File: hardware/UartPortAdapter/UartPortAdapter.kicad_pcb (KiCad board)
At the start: 2 copper layers, 16.5 x 19.5 mm, 3 parts, among them J1 Mid Expansion Header, J2 FTDI

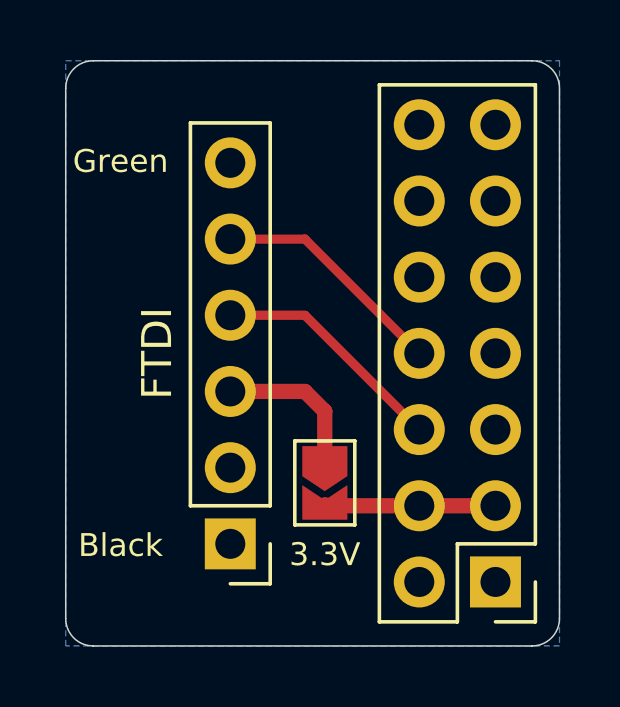
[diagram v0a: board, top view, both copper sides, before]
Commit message: Fixed the UART adapter PCB
The 0.1" 2x7 Mid Expansion header was flipped left to right. I noticed
this issue when testing revision 0.1.0 of the PCB.

This updated version has been sent off to OSHPark for manufacture.
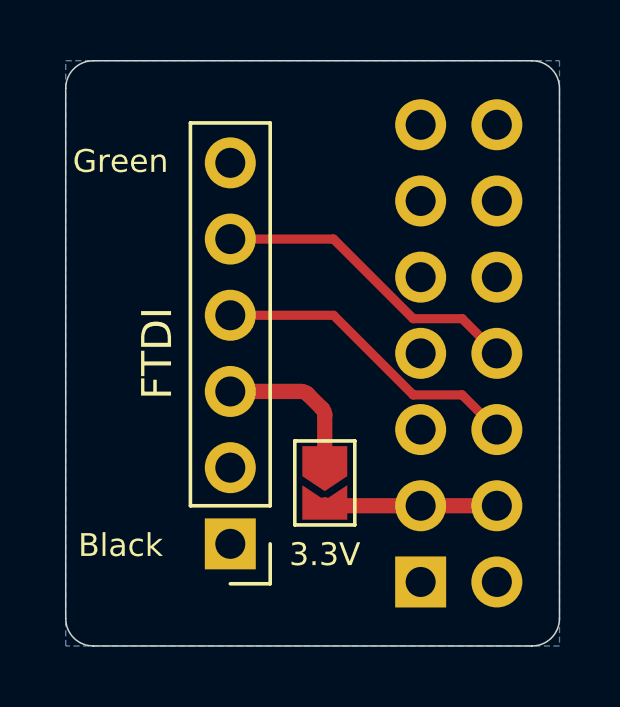
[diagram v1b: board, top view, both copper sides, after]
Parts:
- J1: moved to B.Cu
- moved J1 2.49 mm to (147.5, 100.0), turned to 0 degrees
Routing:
- net Net-(J1-Pad8): track 7.88 -> 10.5 mm
- net Net-(J1-Pad6): track 7.88 -> 10.5 mm
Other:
- board text added: "v 0.2.0"
- board text removed: "v 0.1.0"
